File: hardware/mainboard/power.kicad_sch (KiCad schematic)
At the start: 62 parts, among them U17 AP6230xWU, U3 AP6230xWU, U4 AP6230xWU, U5 SiC438, U6 AP6230xWU, U7 AP6230xWU

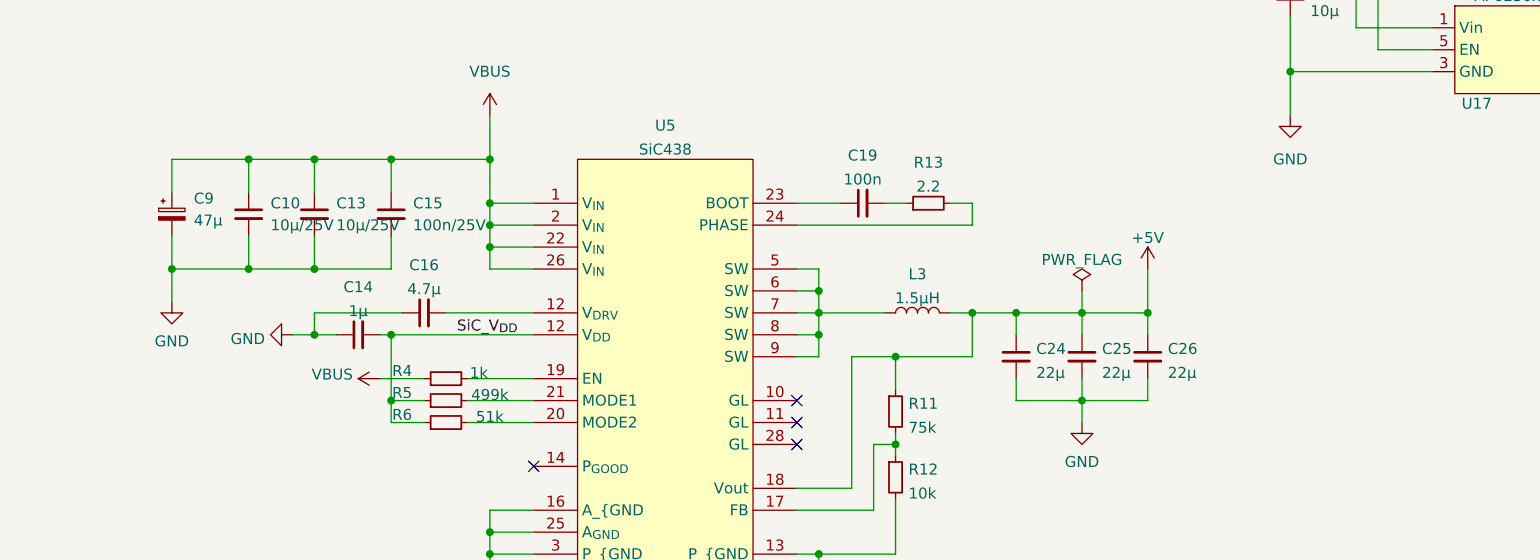
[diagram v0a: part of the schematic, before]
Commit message: Add TVS on 5V and Vbus
Signed-off-by: gatecat <gatecat@ds0.me>
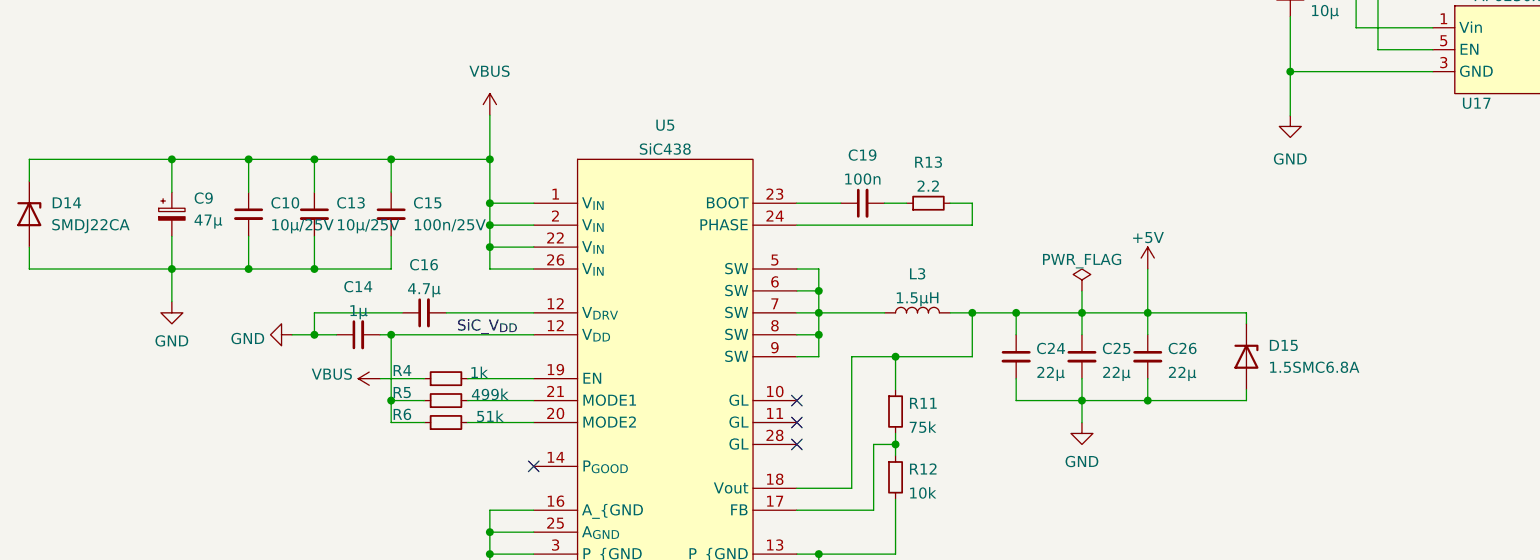
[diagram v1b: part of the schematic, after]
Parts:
- added D14: SMDJ22CA, Diode_SMD:D_SMC, symbol Device:D_Zener
- added D15: 1.5SMC6.8A, Diode_SMD:D_SMC, symbol Device:D_Zener
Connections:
- net +5V: now also D15.1 (K)
- net GND: now also D14.2 (A), D15.2 (A)
- net VBUS: now also D14.1 (K)
